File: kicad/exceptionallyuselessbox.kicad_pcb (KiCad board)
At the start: 2 copper layers, 53.1 x 72.4 mm, 14 parts, among them J1 Conn_01x02, J2 Conn_01x04, J3 Conn_01x02, J4 Conn_01x03, J5 Conn_01x03, U1 DSN-MINI-360

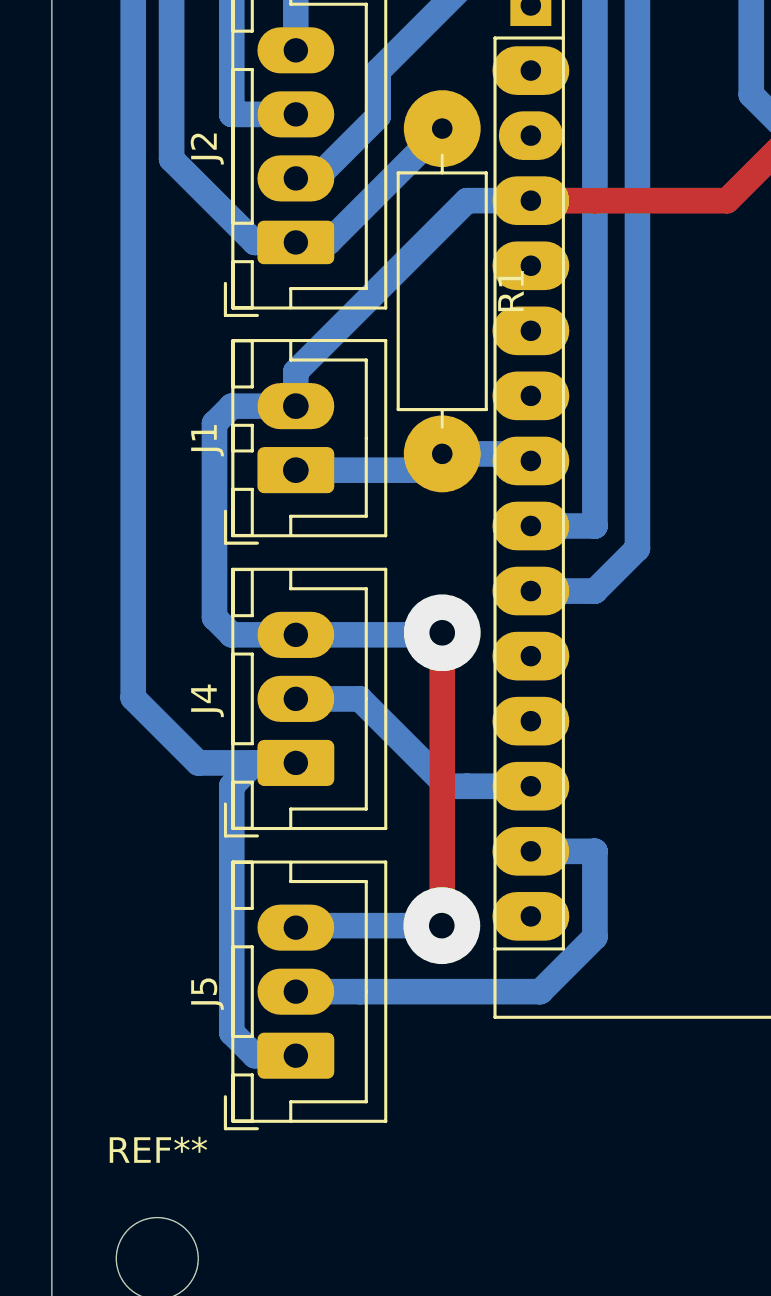
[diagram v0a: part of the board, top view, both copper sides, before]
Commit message: Fix servo pinout.
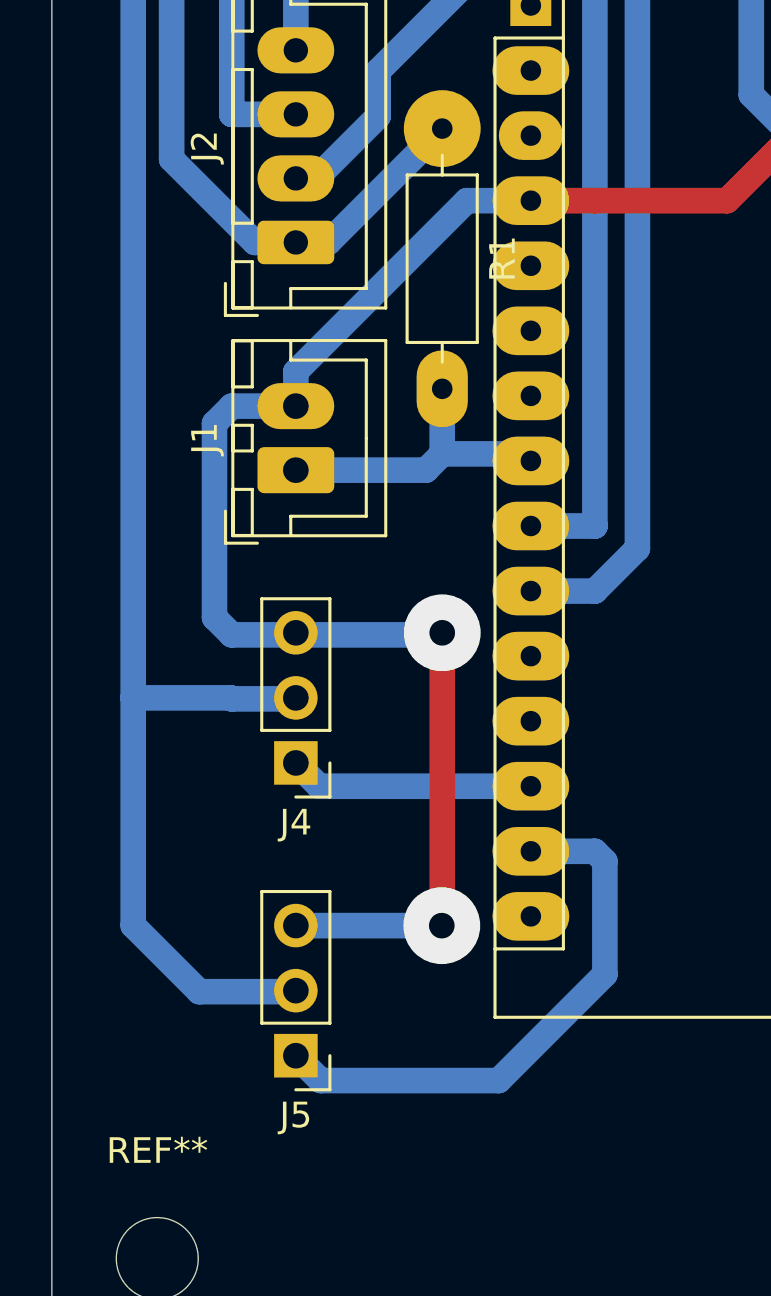
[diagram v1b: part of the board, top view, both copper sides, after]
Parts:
- J4, J5: footprint Connector_JST:JST_XH_B03B-XH-A_1x03_P2.50mm_Vertical -> Connector_PinHeader_2.54mm:PinHeader_1x03_P2.54mm_Vertical
- R1: footprint Resistor_THT:R_Axial_DIN0309_L9.0mm_D3.2mm_P12.70mm_Horizontal -> Resistor_THT:R_Axial_DIN0207_L6.3mm_D2.5mm_P10.16mm_Horizontal
- turned J4 to 180 degrees
- turned J5 to 180 degrees
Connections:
- J4 pad 1: +6V -> TOP
- J4 pad 2: TOP -> +6V
- J5 pad 1: +6V -> BOT
- J5 pad 2: BOT -> +6V
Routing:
- net BOT: track 18.4 -> 21.7 mm
- net Net-(A1-Pad8): track 9.55 -> 12.1 mm
- net TOP: track 10.6 -> 9.55 mm

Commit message: Update PCB.
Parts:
- removed U1: DSN-MINI-360, Module:DSN-MINI-360
- added L1: 10 mH, Inductor_THT:L_Radial_D9.5mm_P5.00mm_Fastron_07HVP, F.Cu at (136.5, 102.9)
- added Q1: IRFZ44N, Package_TO_SOT_THT:TO-220-3_Vertical, F.Cu at (114.3, 137.8)
- added R2: 1K, Resistor_THT:R_Axial_DIN0207_L6.3mm_D2.5mm_P5.08mm_Vertical, F.Cu at (122.6, 135.9)
- added R3: 10K, Resistor_THT:R_Axial_DIN0207_L6.3mm_D2.5mm_P5.08mm_Vertical, F.Cu at (122.6, 141.0)
- moved REF** 5.00 mm to (100.0, 80.0)
- moved REF** 5.00 mm to (145.0, 80.0)
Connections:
- A1 pad 16: Net-(A1-Pad16) -> SERVO_ON
- A1 pad 30: +BATT -> Net-(A1-Pad30)
- C1 pad 1: +BATT -> +5V
- C2 pad 1: +6V -> Net-(C2-Pad1)
- J3 pad 1: +BATT -> +5V
- J4 pad 2: +6V -> Net-(J4-Pad2)
- J5 pad 2: +6V -> Net-(J4-Pad2)
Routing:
- net +6V: track 113.8 -> 0.00 mm
- net Net-(C2-Pad1): track 0.00 -> 90.6 mm
- net +BATT: track 71.7 -> 0.00 mm, vias 2 -> 0
- net Net-(J4-Pad2): track 0.00 -> 51.9 mm
- net +5V: track 64.7 -> 107.5 mm
- net SERVO_ON: track 0.00 -> 15.2 mm
- net Net-(Q1-Pad1): track 0.00 -> 9.04 mm
- net GND: track 151.7 -> 152.7 mm, vias 4 -> 6
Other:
- board size 53.1 x 72.4 mm -> 53.1 x 71 mm
